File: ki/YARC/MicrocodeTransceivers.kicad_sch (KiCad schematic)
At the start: 5 parts, among them U66 74HC245, U67 74LS574, U68 74LS574, U69 74HC245, U70 74HC245

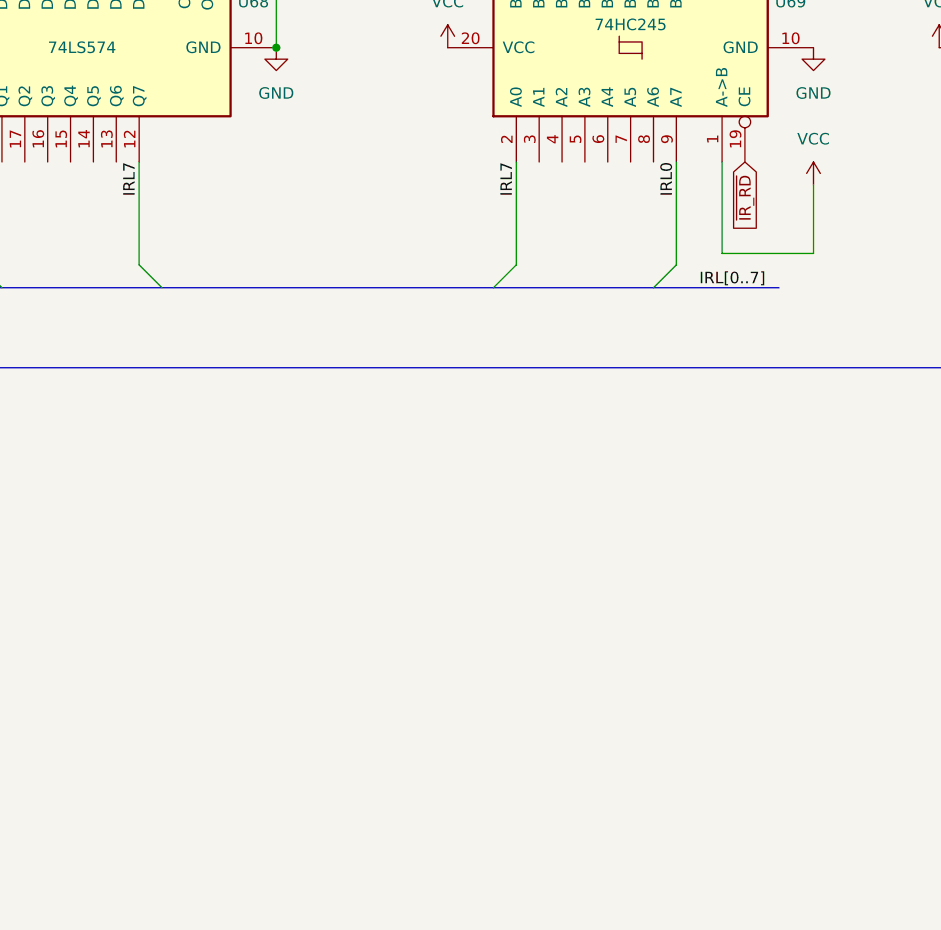
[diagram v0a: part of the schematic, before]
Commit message: Implement ir0_en microcode bit to fix design error with JMP
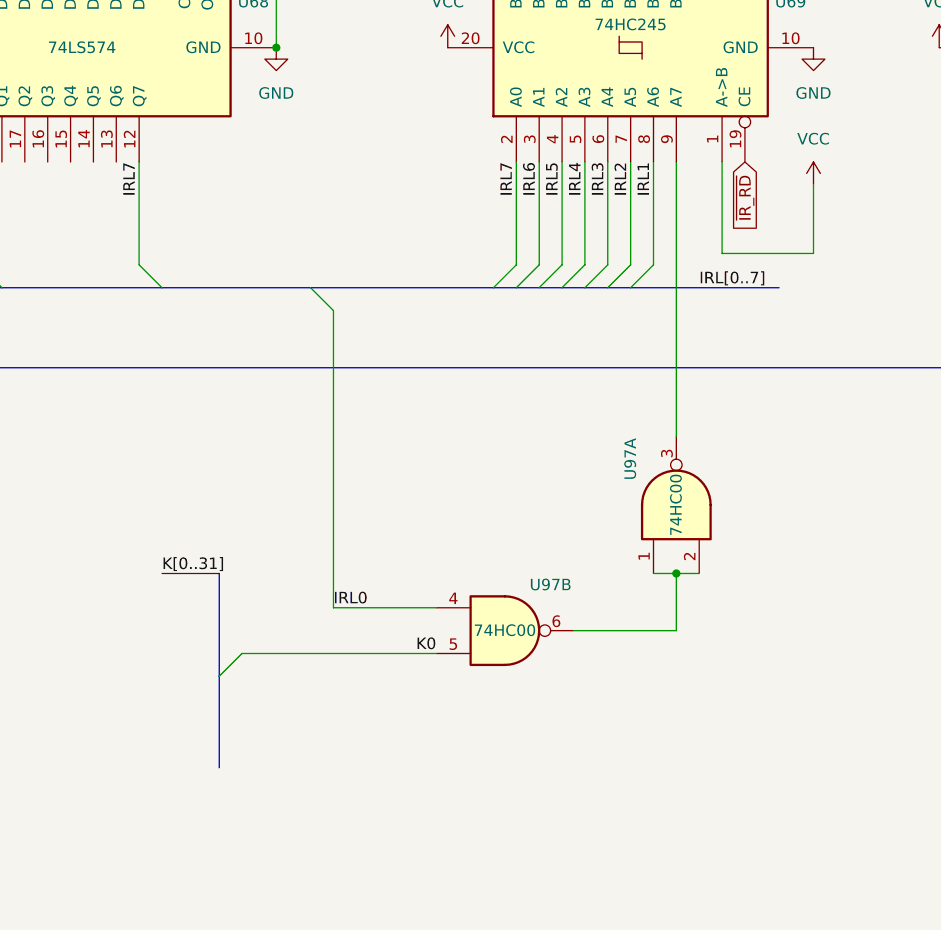
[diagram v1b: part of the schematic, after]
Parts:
- added U97: 74HC00, symbol 74xx:74HC00
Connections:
- net IRL0: now also U97.4; no longer U69.9 (A7)
- net IRL6: now reaches U69.3 (A1)
- net IRL5: now reaches U69.4 (A2)
- net IRL4: now reaches U69.5 (A3)
- net IRL3: now reaches U69.6 (A4)
- net IRL2: now reaches U69.7 (A5)
- net IRL1: now reaches U69.8 (A6)
- new net: U97.1, U97.2, U97.6
- new net: U69.9 (A7), U97.3
- new net K0: U97.5

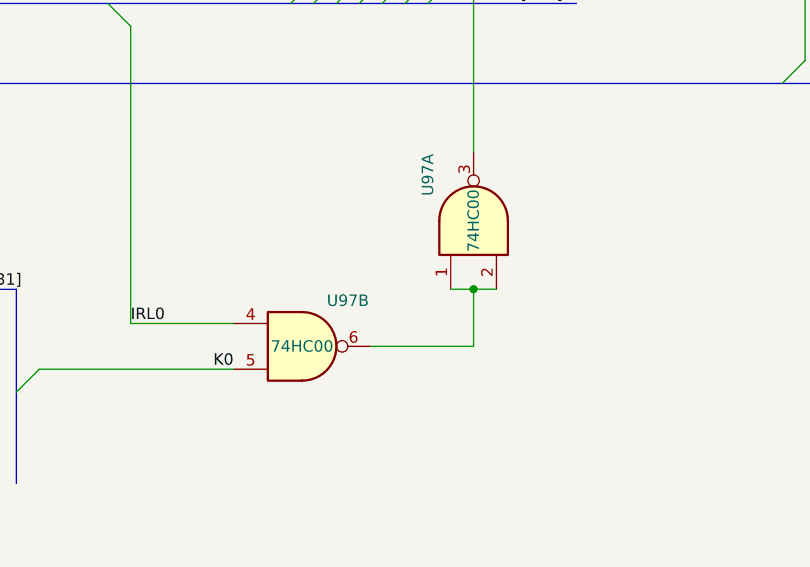
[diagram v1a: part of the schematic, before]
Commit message: Convert schematic to KiCad 7
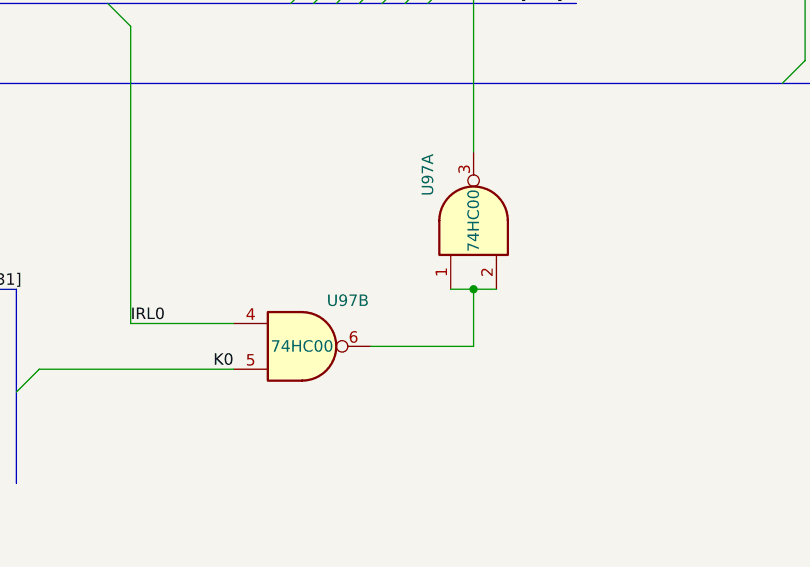
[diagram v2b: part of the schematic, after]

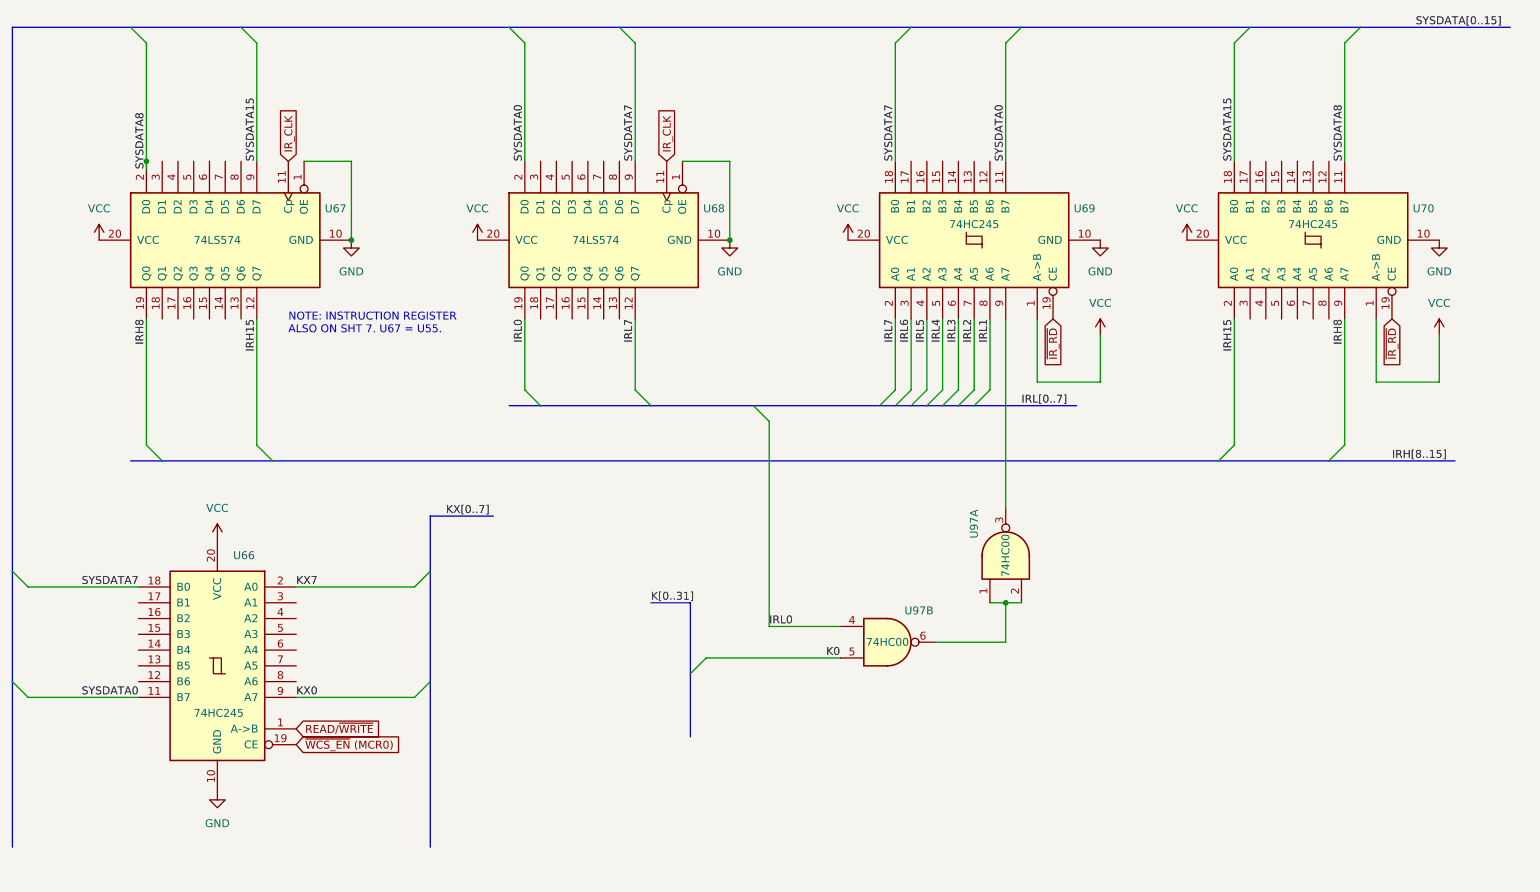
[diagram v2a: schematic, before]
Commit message: Removed about 2/3 of 2300+ errors from the ERC
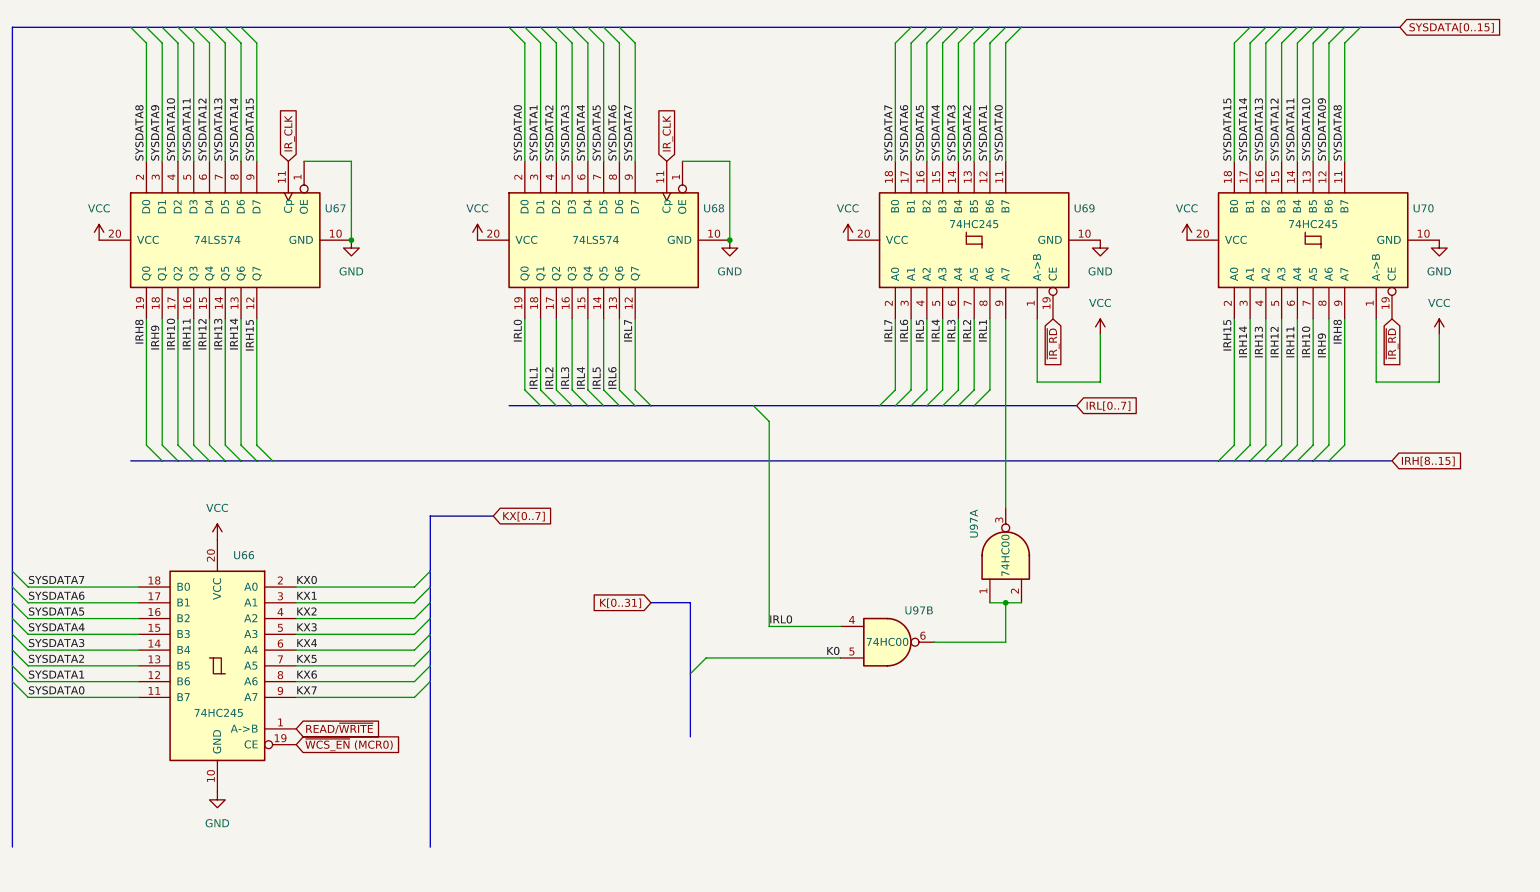
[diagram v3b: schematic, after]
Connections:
- net IRL1: now also U68.18 (Q1)
- net IRL2: now also U68.17 (Q2)
- net IRL3: now also U68.16 (Q3)
- net IRL4: now also U68.15 (Q4)
- net IRL5: now also U68.14 (Q5)
- net IRL6: now also U68.13 (Q6)
- net KX0: now also U66.2 (A0); no longer U66.9 (A7)
- net KX7: now also U66.9 (A7); no longer U66.2 (A0)
- net SYSDATA1: now reaches U68.3 (D1)
- net SYSDATA1: now also U66.12 (B6), U69.12 (B6)
- net SYSDATA2: now reaches U68.4 (D2)
- net SYSDATA2: now also U66.13 (B5), U69.13 (B5)
- net SYSDATA3: now reaches U68.5 (D3)
- net SYSDATA3: now also U66.14 (B4), U69.14 (B4)
- net SYSDATA4: now reaches U68.6 (D4)
- net SYSDATA4: now also U66.15 (B3), U69.15 (B3)
- net SYSDATA5: now reaches U68.7 (D5)
- net SYSDATA5: now also U66.16 (B2), U69.16 (B2)
- net SYSDATA6: now reaches U68.8 (D6)
- net SYSDATA6: now also U66.17 (B1), U69.17 (B1)
- net IRH14: now reaches U67.13 (Q6)
- net IRH14: now also U70.3 (A1)
- net IRH13: now reaches U67.14 (Q5)
- net IRH13: now also U70.4 (A2)
- net IRH12: now reaches U67.15 (Q4)
- net IRH12: now also U70.5 (A3)
- net IRH11: now reaches U67.16 (Q3)
- net IRH11: now also U70.6 (A4)
- net IRH10: now reaches U67.17 (Q2)
- net IRH10: now also U70.7 (A5)
- net IRH9: now reaches U67.18 (Q1)
- net IRH9: now also U70.8 (A6)
- net SYSDATA9: now reaches U67.3 (D1)
- net SYSDATA10: now reaches U67.4 (D2)
- net SYSDATA10: now also U70.13 (B5)
- net SYSDATA11: now reaches U67.5 (D3)
- net SYSDATA11: now also U70.14 (B4)
- net SYSDATA12: now reaches U67.6 (D4)
- net SYSDATA12: now also U70.15 (B3)
- net SYSDATA13: now reaches U67.7 (D5)
- net SYSDATA13: now also U70.16 (B2)
- net SYSDATA14: now reaches U67.8 (D6)
- net SYSDATA14: now also U70.17 (B1)
- net KX1: now reaches U66.3 (A1)
- net KX2: now reaches U66.4 (A2)
- net KX3: now reaches U66.5 (A3)
- net KX4: now reaches U66.6 (A4)
- net KX5: now reaches U66.7 (A5)
- net KX6: now reaches U66.8 (A6)
- net SYSDATA09: now reaches U70.12 (B6)
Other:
- note removed: "NOTE: INSTRUCTION REGISTER ALSO ON SHT 7. U67 = U55."

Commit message: Ongoing fixes for ERC errors
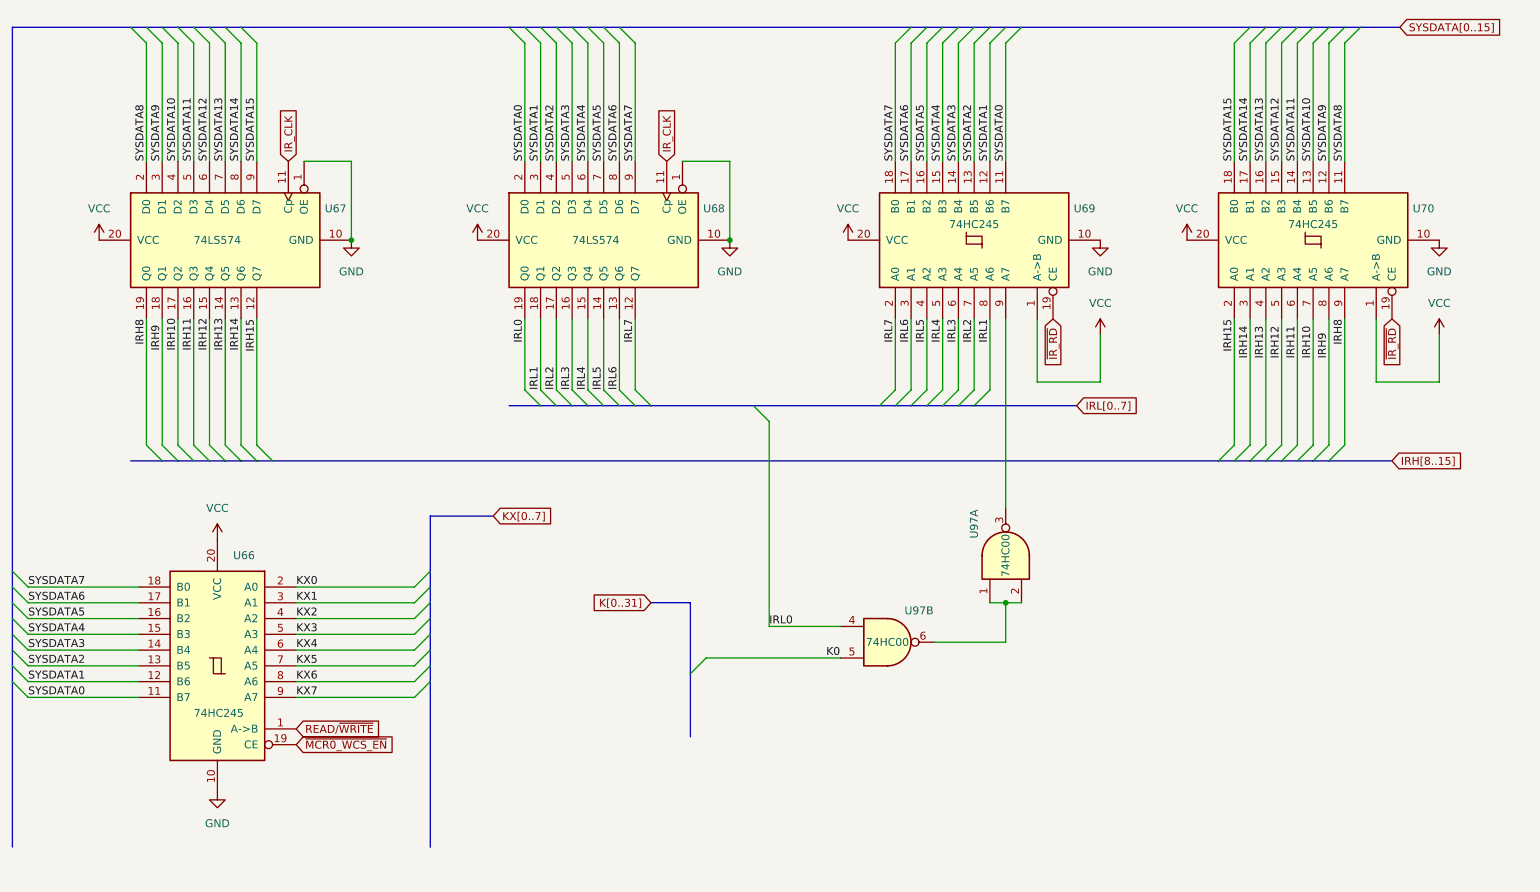
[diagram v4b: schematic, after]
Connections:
- net SYSDATA09 is gone; now on net SYSDATA9: U70.12 (B6)
- net ~{WCS_EN} (MCR0) renamed ~{MCR0_WCS_EN}
